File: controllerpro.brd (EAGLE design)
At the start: 83.8 x 37.5 mm, 10 parts, among them IC1 MCP1703CB, IC2 741G3157DBVR, IC3 741G3157DBVR, IC4 741G3157DBVR, IC5 741G3157DBVR

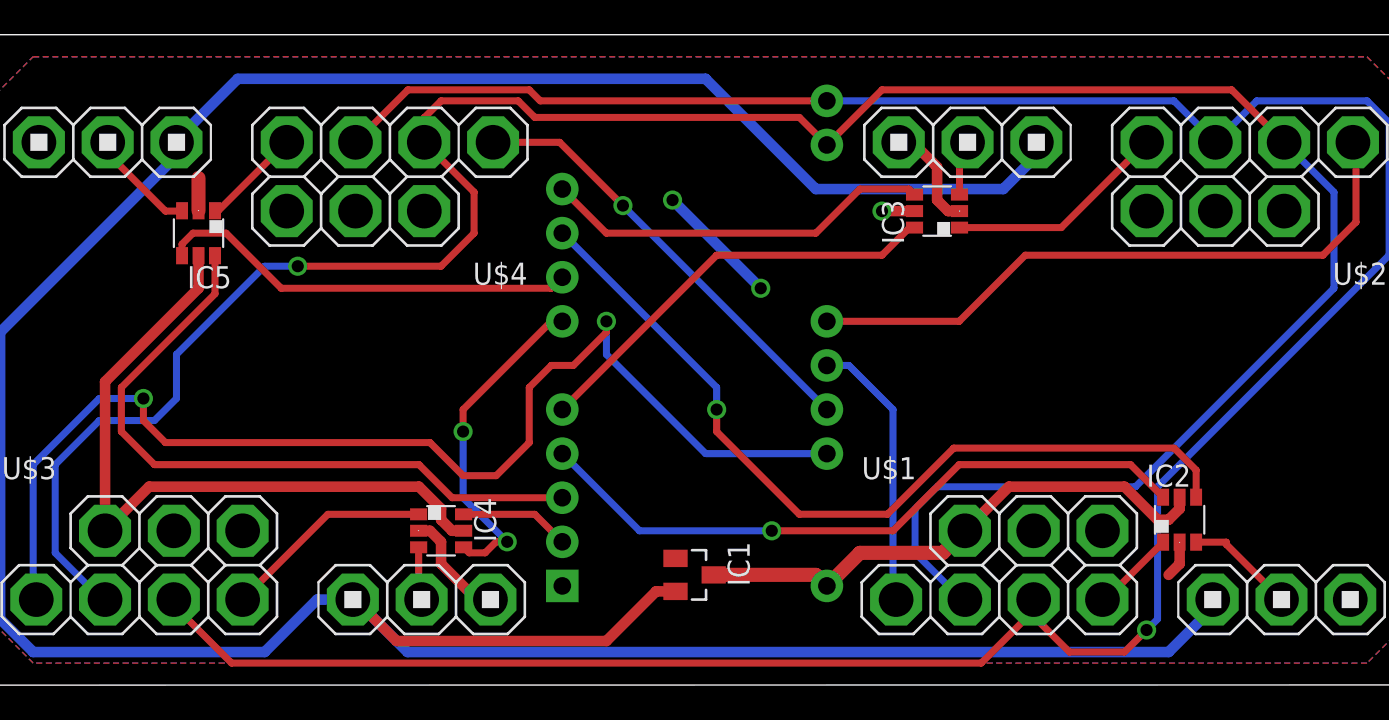
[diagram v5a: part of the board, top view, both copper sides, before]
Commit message: Adding pull-up resistors
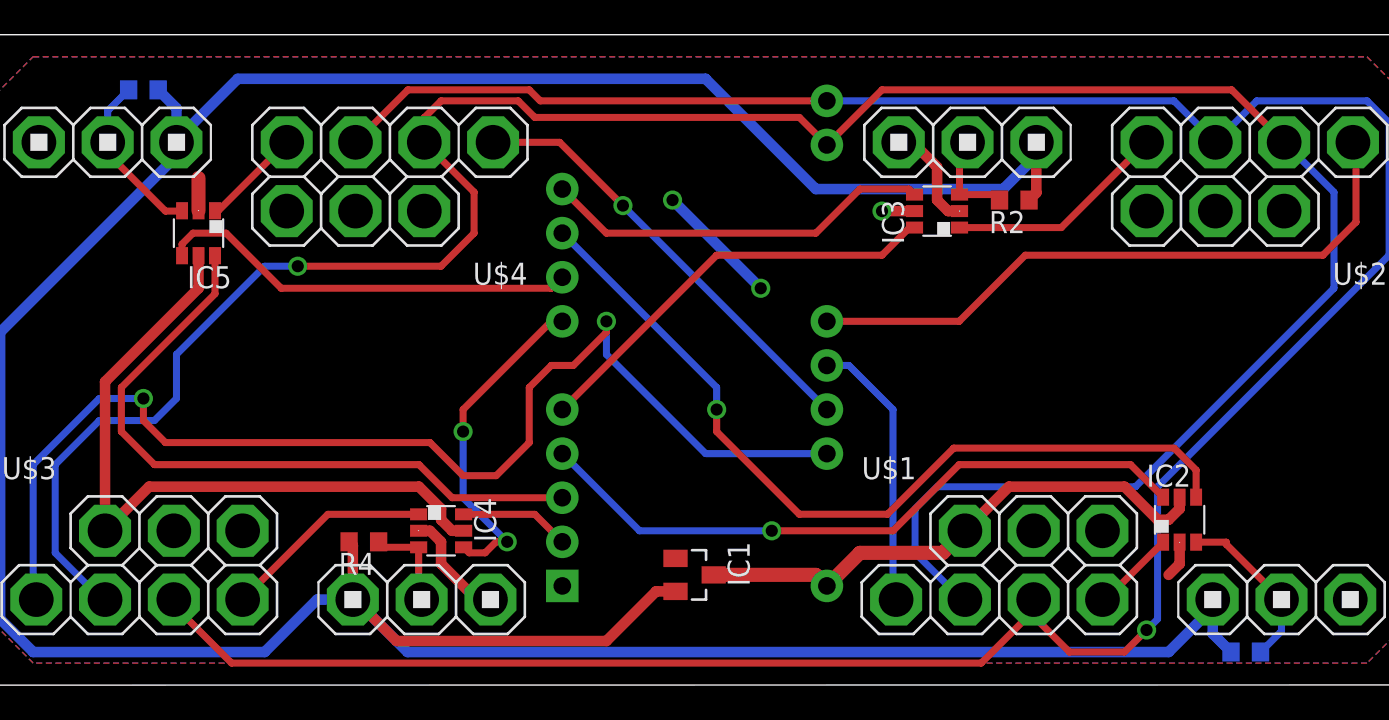
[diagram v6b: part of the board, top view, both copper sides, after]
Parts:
- added R1, R2, R3, R4: (no value), rcl:R0603
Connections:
- net N$12: now also R2.2
- net N$14: now also R4.1
- net N$7: now also R1.2
- net N$8: now also R3.1
- net V33: now also R1.1, R2.1, R3.2, R4.2
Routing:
- net V33: track 182.4 -> 196.3 mm
- net N$7: track 6.30 -> 9.83 mm
- net N$8: track 6.36 -> 9.88 mm
- net N$14: track 3.08 -> 5.52 mm
- net N$12: track 3.28 -> 5.71 mm
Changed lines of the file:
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@@
 <element name="IC5" library="74xx-little-de" package="DBV_R-PDSO-G6" value="741G3157DBVR" x="13.335" y="26.035" rot="R180"/>
 <element name="U$5" library="custom" package="TEENSY_MC_PINS" value="TEENSY_MC_PINS" x="41.91" y="19.685" rot="MR90"/>
+<element name="R1" library="rcl" package="R0603" value="" x="10.16" y="34.29" rot="MR0"/>
+<element name="R2" library="rcl" package="R0603" value="" x="60.325" y="27.94" rot="R180"/>
+<element name="R3" library="rcl" package="R0603" value="" x="73.66" y="1.905" rot="MR0"/>
+<element name="R4" library="rcl" package="R0603" value="" x="22.86" y="8.255" rot="R180"/>
 </elements>
 <signals>
@@
 <wire x1="22.8473" y1="4.4323" x2="22.7203" y2="4.4323" width="0.6096" layer="1"/>
 <wire x1="22.7203" y1="4.4323" x2="22.225" y2="4.9276" width="0.6096" layer="1"/>
+<contactref element="R3" pad="2"/>
+<contactref element="R2" pad="1"/>
+<contactref element="R1" pad="1"/>
+<contactref element="R4" pad="2"/>
+<wire x1="11.01" y1="34.29" x2="12.065" y2="33.235" width="0.6096" layer="16"/>
+<wire x1="12.065" y1="33.235" x2="12.065" y2="31.2674" width="0.6096" layer="16"/>
+<wire x1="22.01" y1="8.255" x2="22.225" y2="8.04" width="0.6096" layer="1"/>
+<wire x1="22.225" y1="8.04" x2="22.225" y2="4.9276" width="0.6096" layer="1"/>
+<wire x1="72.81" y1="1.905" x2="71.755" y2="2.96" width="0.6096" layer="16"/>
+<wire x1="71.755" y1="2.96" x2="71.755" y2="4.9276" width="0.6096" layer="16"/>
+<wire x1="61.175" y1="27.94" x2="61.595" y2="28.36" width="0.6096" layer="1"/>
+<wire x1="61.595" y1="28.36" x2="61.595" y2="31.2674" width="0.6096" layer="1"/>
 </signal>
 <signal name="N$5">
@@
 <wire x1="8.255" y1="30.48" x2="8.255" y2="31.115" width="0.4064" layer="1"/>
 <wire x1="8.255" y1="31.115" x2="8.1026" y2="31.2674" width="0.4064" layer="1"/>
+<contactref element="R1" pad="2"/>
+<wire x1="8.1026" y1="31.2674" x2="8.1026" y2="33.0826" width="0.4064" layer="16"/>
+<wire x1="8.1026" y1="33.0826" x2="9.31" y2="34.29" width="0.4064" layer="16"/>
 </signal>
 <signal name="N$8">
@@
 <wire x1="72.537" y1="8.235" x2="72.537" y2="8.108" width="0.4064" layer="1"/>
 <wire x1="72.537" y1="8.108" x2="75.7174" y2="4.9276" width="0.4064" layer="1"/>
+<contactref element="R3" pad="1"/>
+<wire x1="74.51" y1="1.905" x2="75.7174" y2="3.1124" width="0.4064" layer="16"/>
+<wire x1="75.7174" y1="3.1124" x2="75.7174" y2="4.9276" width="0.4064" layer="16"/>
 </signal>
 <signal name="N$9">
@@
 <wire x1="57.17" y1="30.9318" x2="57.297" y2="30.9318" width="0.4064" layer="1"/>
 <wire x1="57.297" y1="30.9318" x2="57.6326" y2="31.2674" width="0.4064" layer="1"/>
+<contactref element="R2" pad="2"/>
+<wire x1="57.17" y1="28.255" x2="59.16" y2="28.255" width="0.4064" layer="1"/>
+<wire x1="59.16" y1="28.255" x2="59.475" y2="27.94" width="0.4064" layer="1"/>
 </signal>
 <signal name="N64_OR_NES0">
@@
 <wire x1="26.015" y1="7.94" x2="26.015" y2="5.1" width="0.4064" layer="1"/>
 <wire x1="26.015" y1="5.1" x2="26.1874" y2="4.9276" width="0.4064" layer="1"/>
+<contactref element="R4" pad="1"/>
+<wire x1="23.71" y1="8.255" x2="24.025" y2="7.94" width="0.4064" layer="1"/>
+<wire x1="24.025" y1="7.94" x2="26.015" y2="7.94" width="0.4064" layer="1"/>
 </signal>
 <signal name="N$15">
@@
 </signal>
 </signals>
+<errors>
+</errors>
 </board>
 </drawing>

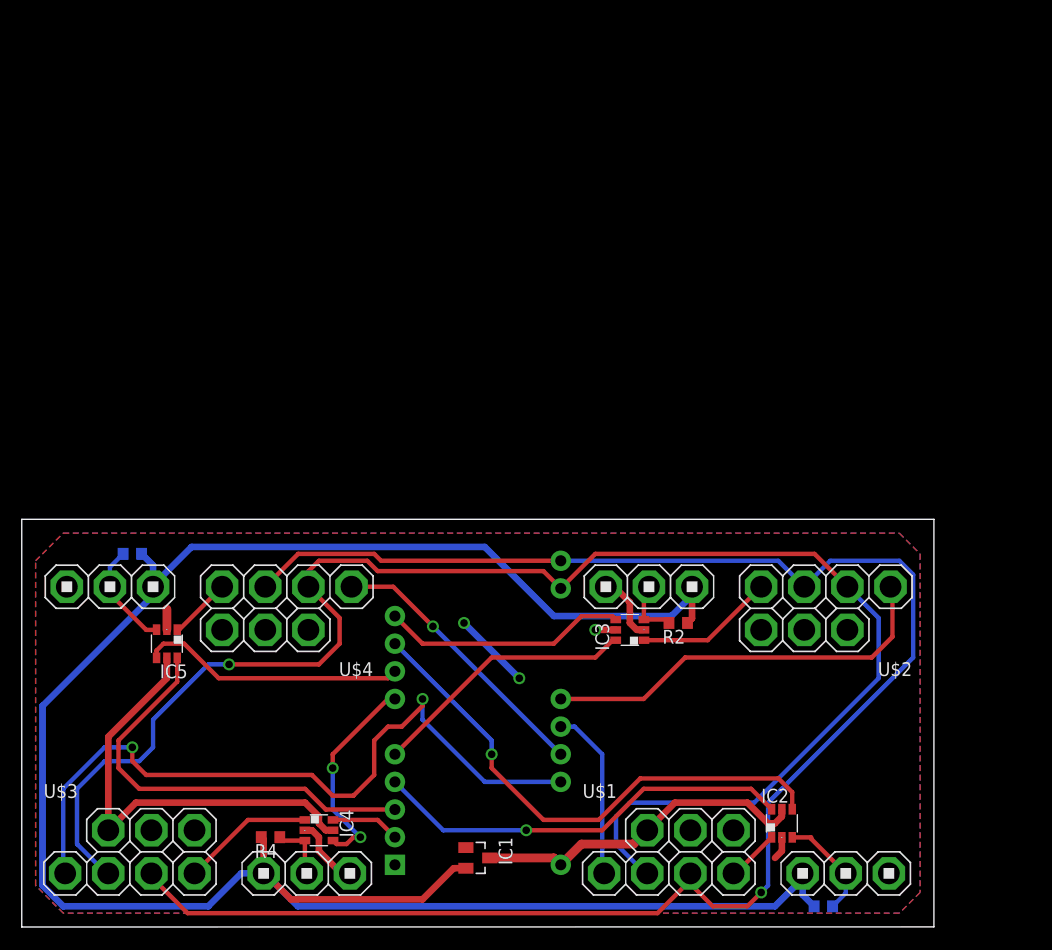
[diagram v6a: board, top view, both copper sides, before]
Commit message: Moving controllers father away from the teensy
Avoiding socket collisions per model
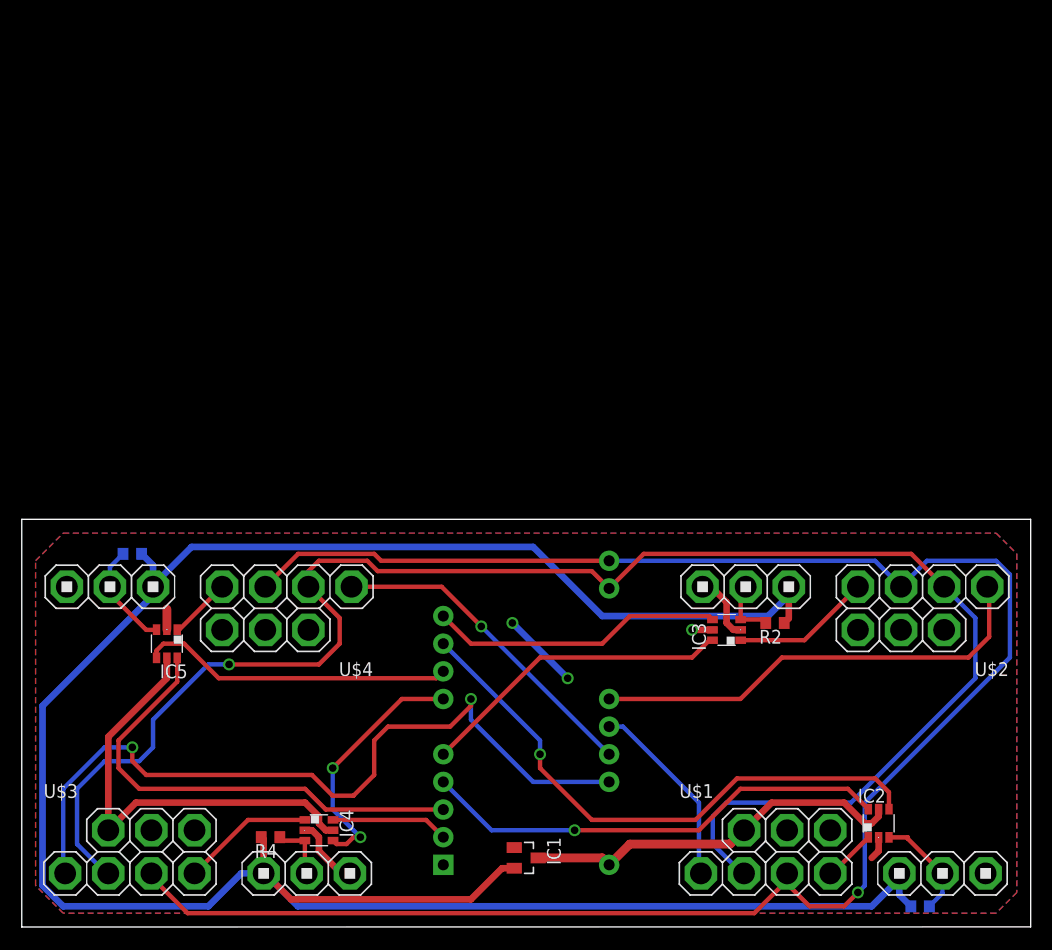
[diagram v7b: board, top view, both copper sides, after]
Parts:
- moved IC2 8.89 mm to (78.7, 9.53)
- moved R2 8.89 mm to (69.2, 27.9)
- moved R3 8.89 mm to (82.5, 1.91)
- moved U$1 8.89 mm to (74.3, 8.89)
- moved U$2 8.89 mm to (76.8, 27.3)
- moved IC3 8.89 mm to (64.8, 27.3)
- moved IC1 4.45 mm to (46.4, 6.35)
- moved U$5 4.45 mm to (46.4, 19.7)
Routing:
- net V33: track 196.3 -> 218.5 mm
- net LATCH: track 159.8 -> 177.6 mm
- net CLOCK: track 147.3 -> 156.2 mm
- net VCC: track 74.6 -> 79.0 mm
- net S_OR_NES1: track 37.5 -> 42.0 mm
- net DATA0: track 48.4 -> 52.8 mm
- net S_OR_NES3: track 25.6 -> 30.0 mm
- net N64_OR_NES2: track 6.34 -> 10.8 mm
- net N64_OR_NES1: track 24.6 -> 29.1 mm
- net N64_OR_NES0: track 38.8 -> 43.3 mm
- net DATA3: track 24.4 -> 28.9 mm
- net DATA1: track 22.5 -> 27.0 mm
- net S_OR_NES2: track 67.9 -> 72.4 mm
- net N64_OR_NES3: track 39.3 -> 43.8 mm
- net DATA2: track 19.4 -> 23.1 mm
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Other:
- board size 83.8 x 37.5 mm -> 92.7 x 37.5 mm

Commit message: Finishing moving controller ports closer together
Also added plugin spot on model
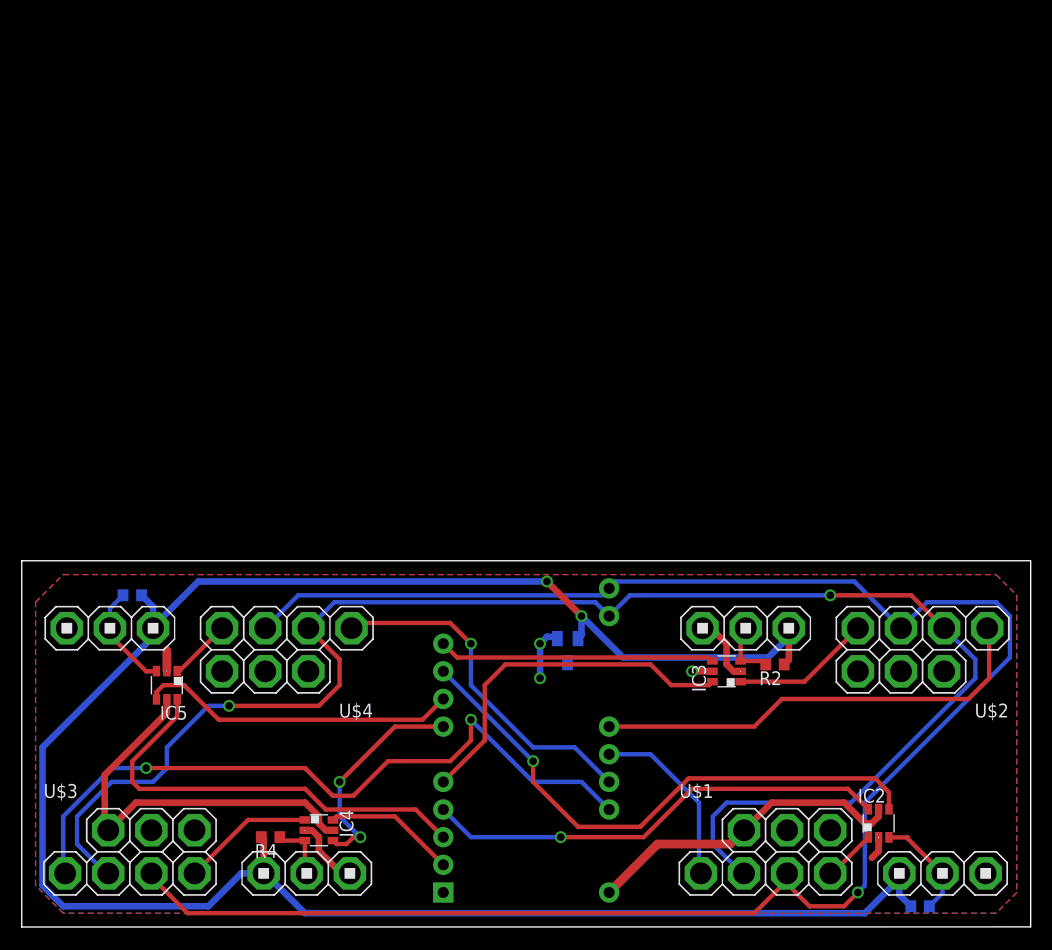
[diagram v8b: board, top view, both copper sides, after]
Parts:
- R1, R2, R3, R4: value (none) -> 10k
- moved IC1 19.4 mm to (50.2, 25.4), flipped to the bottom, turned to 180 degrees
- moved R2 3.81 mm to (69.2, 24.1)
- moved IC3 3.81 mm to (64.8, 23.5)
- moved IC5 3.81 mm to (13.3, 22.2)
- moved R1 3.81 mm to (10.2, 30.5)
- moved U$2 3.81 mm to (76.8, 23.5)
- moved U$4 3.81 mm to (18.4, 23.5)
- moved U$5 2.54 mm to (46.4, 17.1)
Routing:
- net V33: track 218.5 -> 192.6 mm, vias 0 -> 2
- net VCC: track 79.0 -> 69.8 mm
- net CLOCK: track 156.2 -> 147.0 mm, vias 1 -> 2
- net S_OR_NES2: track 72.4 -> 65.8 mm
- net N64_OR_NES1: track 29.1 -> 33.1 mm
- net N64_OR_NES3: track 43.8 -> 40.0 mm
- net LATCH: track 177.6 -> 174.8 mm
- net DATA2: track 23.1 -> 20.4 mm
- net S_OR_NES3: track 30.0 -> 32.2 mm
- net GND: track 24.0 -> 21.9 mm
- net DATA1: track 27.0 -> 25.4 mm
- net N64_OR_NES2: track 10.8 -> 12.1 mm
- net S_OR_NES0: track 17.7 -> 16.7 mm
- net DATA0: track 52.8 -> 51.9 mm
- net S_OR_NES1: track 42.0 -> 41.4 mm
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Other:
- board size 92.7 x 37.5 mm -> 92.7 x 33.7 mm
